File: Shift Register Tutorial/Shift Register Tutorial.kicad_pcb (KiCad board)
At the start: 2 copper layers, 134.6 x 162.6 mm, 58 parts, among them J101 USB_A, Q201 2N3904, Q301 2N3904, Q401 2N3904, SW201 SW_Push, SW301 SW_Push, SW401 SW_Push, U101 74164, U102 74164

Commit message: Some adjustments
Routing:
- net +5V: track 30.8 -> 0.00 mm, vias 8 -> 0
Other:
- outline, holes or cut-outs redrawn
- board text added: "Chained Shift Registers"

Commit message: Final tweaks
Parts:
- moved C201 6.35 mm to (-57.1, -52.1)
- moved D201 6.35 mm to (-47.0, -43.2)
- moved D401 6.35 mm to (-47.0, 33.0)
- moved Q201 6.35 mm to (-47.0, -34.3)
- moved R201 6.35 mm to (-57.1, -47.0)
- moved R202 6.35 mm to (-57.1, -36.8)
- moved R203 6.35 mm to (-52.1, -47.0)
- moved R301 6.35 mm to (-57.1, -11.4)
- moved R303 6.35 mm to (-52.1, -11.4)
- moved R401 6.35 mm to (-57.1, 19.1)
- moved R402 6.35 mm to (-57.1, 29.2)
- moved R403 6.35 mm to (-52.1, 19.1)
- moved SW201 6.35 mm to (-68.6, -45.7)
- moved SW301 6.35 mm to (-68.6, -10.2)
- moved SW401 6.35 mm to (-68.6, 30.5)
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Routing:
- net /Data/DATA: track 79.4 -> 72.7 mm
- net /Clock/CLOCK: track 219.3 -> 224.2 mm
- net /~RESET/~RESET: track 209.8 -> 209.1 mm
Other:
- board size 134.6 x 162.6 mm -> 133.3 x 156.2 mm
- board text added: "Debounce"
- board text added: "JLCJLCJLCJLC"
- board text added: "RGE2021"

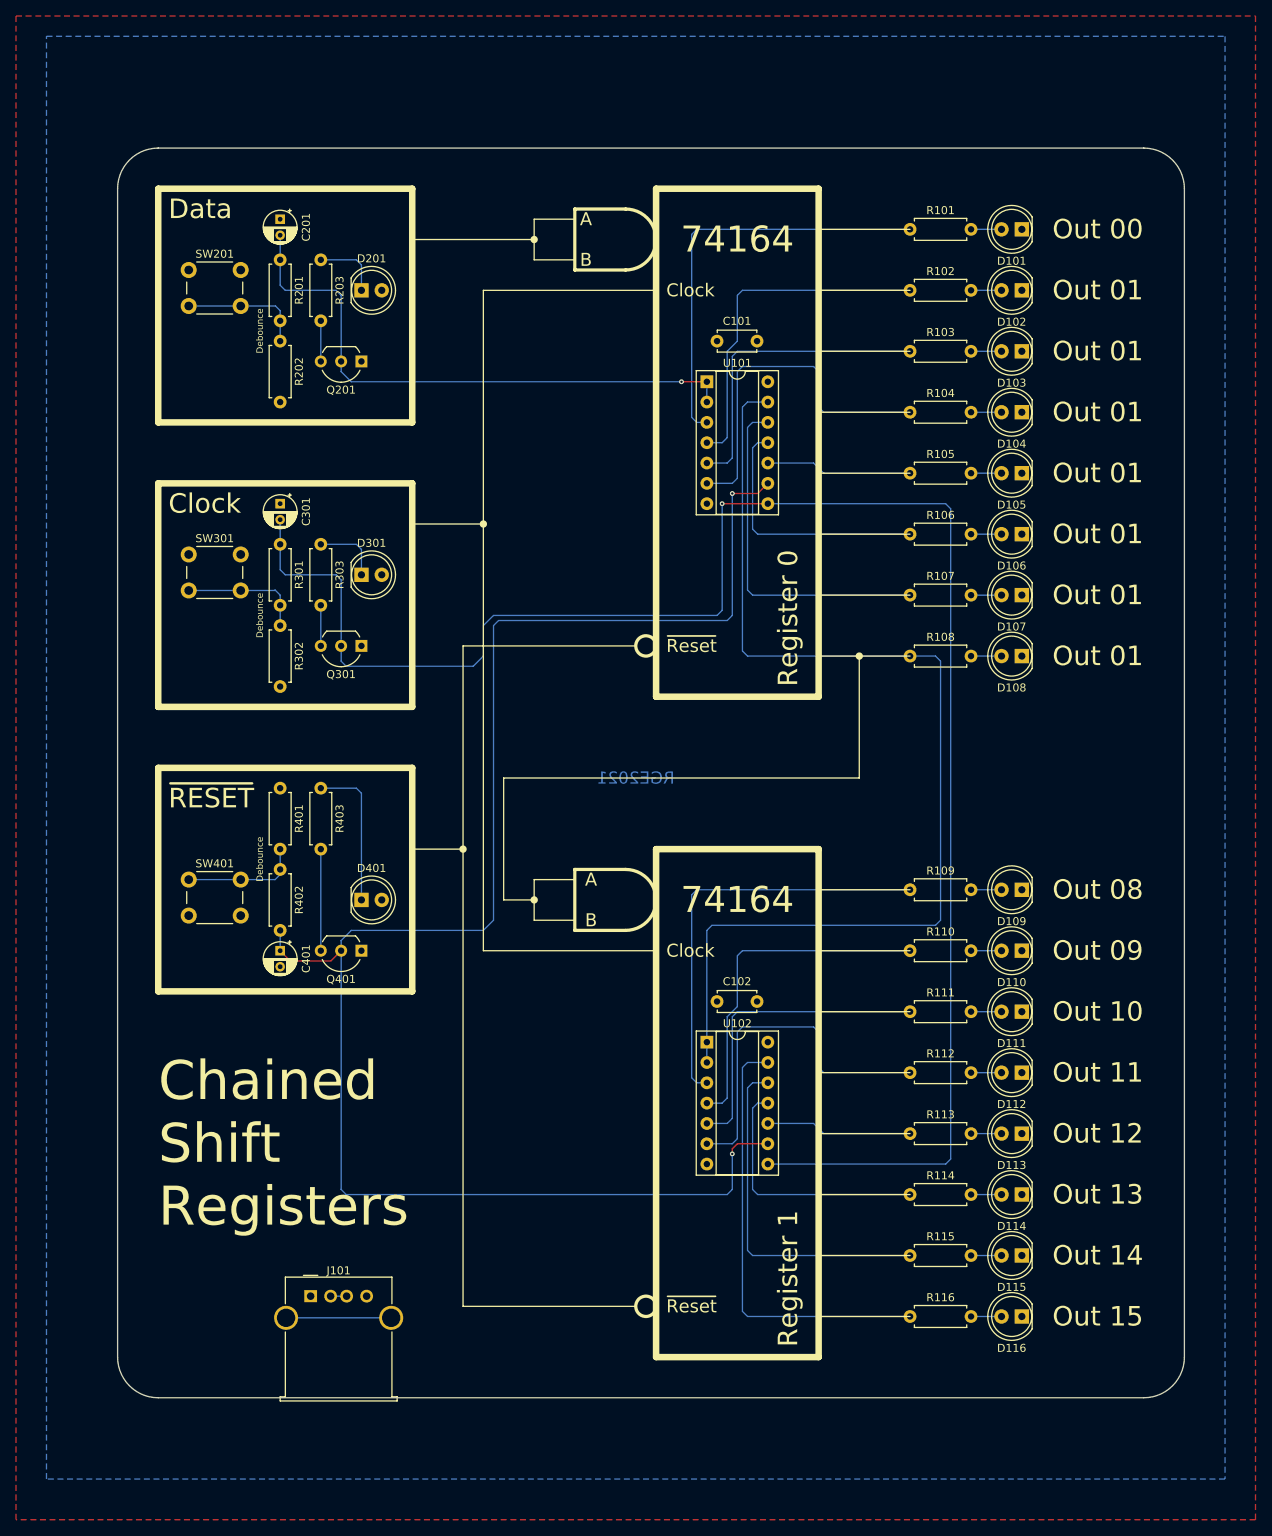
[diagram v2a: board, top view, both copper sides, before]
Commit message: Fix shift register tutorial (#11)
I had forgotten how NPN transistors worked, which resulted in the push buttons not affecting their target pins. Remove the transistors & indicator LEDs, and shrink the board.
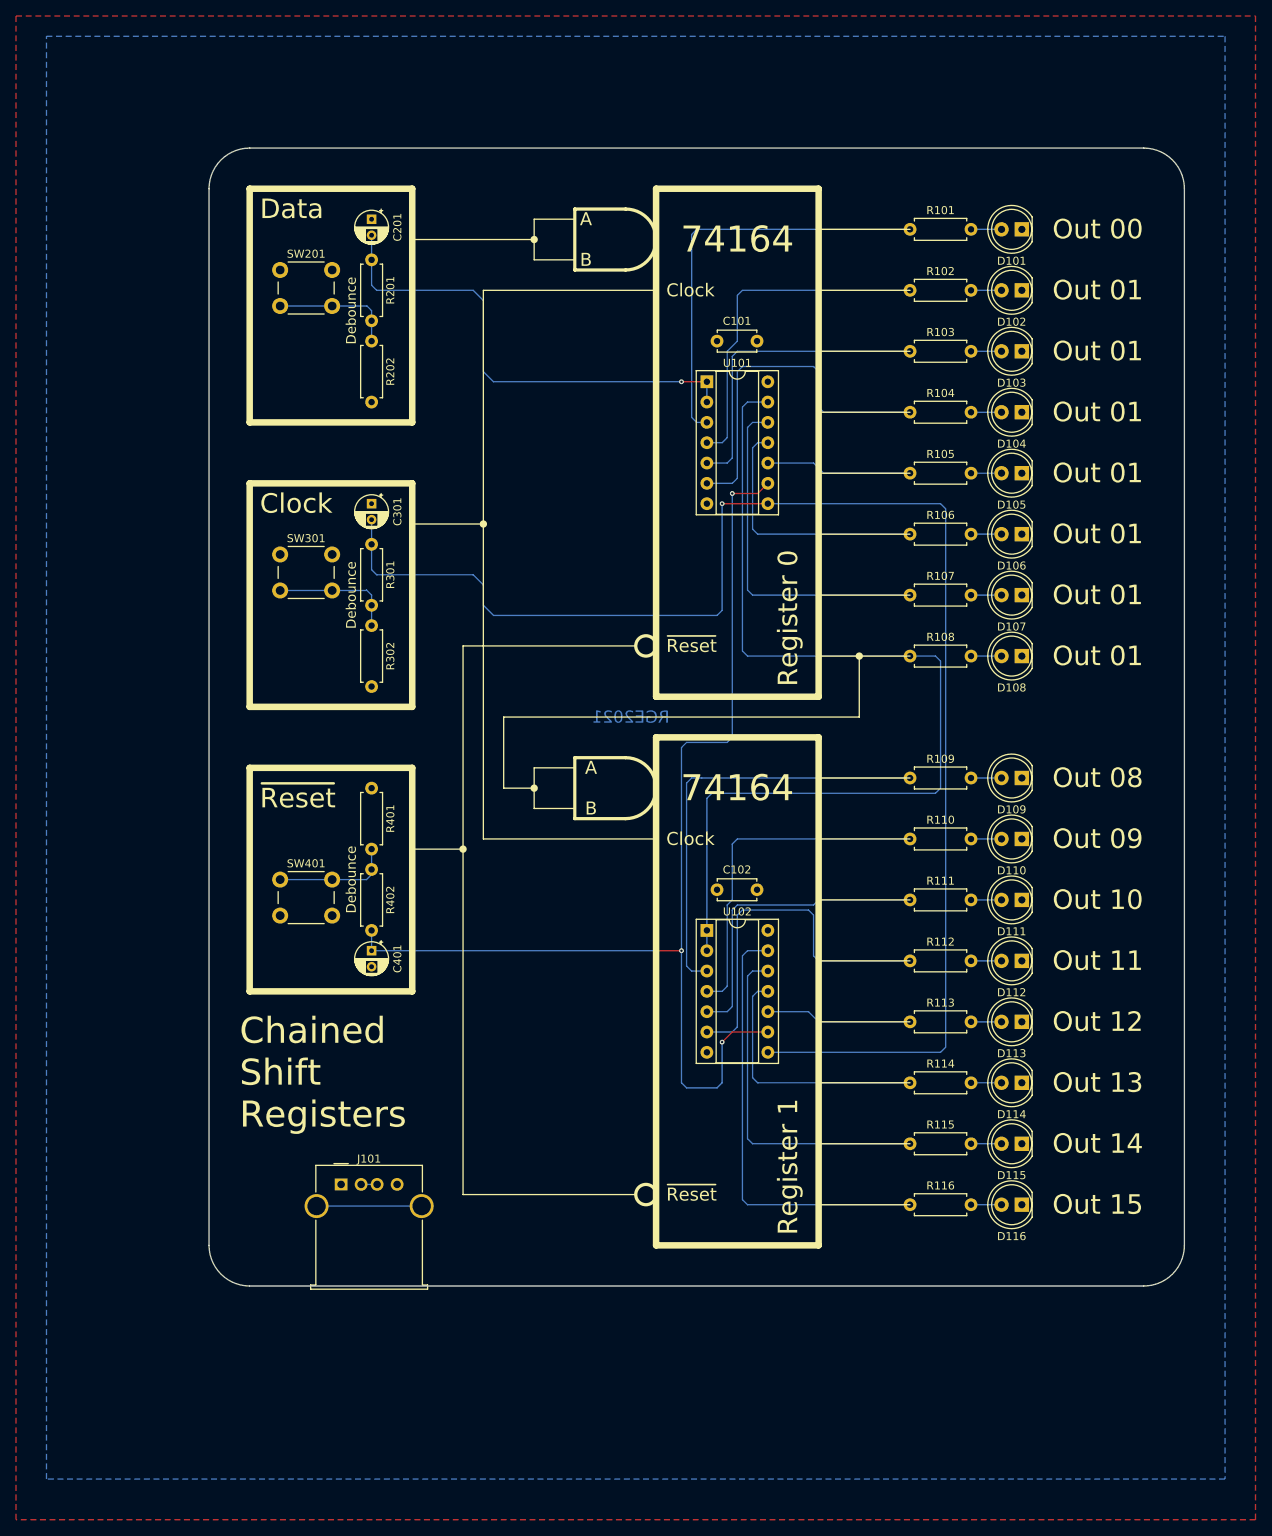
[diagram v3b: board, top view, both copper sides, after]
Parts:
- removed D201, D301, D401: LED, LED_THT:LED_D5.0mm
- removed Q201, Q301, Q401: 2N3904, Package_TO_SOT_THT:TO-92_Inline_Wide
- removed R203, R303, R403: 2k2, Resistor_THT:R_Axial_DIN0207_L6.3mm_D2.5mm_P7.62mm_Horizontal
- C201, C301, C401: value 1u -> 10u
- moved J101 14.5 mm to (-49.5, 68.6)
- moved C102 14.0 mm to (-2.54, 31.8)
- moved D109 14.0 mm to (35.6, 17.8)
- moved D110 14.0 mm to (35.6, 25.4)
- moved D111 14.0 mm to (35.6, 33.0)
- moved D112 14.0 mm to (35.6, 40.6)
- moved D113 14.0 mm to (35.6, 48.3)
- moved D115 14.0 mm to (35.6, 63.5)
- moved D116 14.0 mm to (35.6, 71.1)
- moved R109 14.0 mm to (21.6, 17.8)
- moved R110 14.0 mm to (21.6, 25.4)
- moved R111 14.0 mm to (21.6, 33.0)
- moved R112 14.0 mm to (21.6, 40.6)
- moved R113 14.0 mm to (21.6, 48.3)
- moved R115 14.0 mm to (21.6, 63.5)
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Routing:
- net /~RESET/~RESET: track 209.1 -> 142.4 mm, vias 2 -> 4
- net /Clock/CLOCK: track 224.2 -> 185.5 mm
- net Net-(D401-Pad1): track 18.7 -> 0.00 mm
- net Net-(R108-Pad1): track 137.8 -> 123.9 mm
- net Net-(Q401-Pad3): track 12.7 -> 0.00 mm
- net /Data/DATA: track 72.7 -> 60.9 mm
- net Net-(D301-Pad1): track 8.52 -> 0.00 mm
- net Net-(D201-Pad1): track 8.52 -> 0.00 mm
- net Net-(Q301-Pad3): track 5.08 -> 0.00 mm
- net Net-(Q201-Pad3): track 5.08 -> 0.00 mm
- net Net-(R112-Pad1): track 44.2 -> 45.5 mm
- net Net-(R109-Pad1): track 52.6 -> 53.9 mm
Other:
- board size 133.3 x 156.2 mm -> 121.9 x 142.2 mm
- board text removed: "~RESET"

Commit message: Removing old things
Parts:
- removed C201, C401: 10u, Capacitor_THT:CP_Radial_D4.0mm_P2.00mm
- removed R202: 10k, Resistor_THT:R_Axial_DIN0207_L6.3mm_D2.5mm_P7.62mm_Horizontal
- removed the R401 at (-45.7, 19.1)
- renumbered R402 to R401
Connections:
- R201 pad 2: Net-(R201-Pad2) -> GND
- R401 pad 1: Net-(R401-Pad2) -> +5V
- SW201 pad 1: +5V -> /Data/DATA
- SW201 pad 2: Net-(R201-Pad2) -> +5V
- SW401 pad 1: Net-(R401-Pad2) -> GND
- SW401 pad 2: GND -> /~RESET/~RESET
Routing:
- net /~RESET/~RESET: track 142.4 -> 104.3 mm
- net /Clock/CLOCK: track 185.5 -> 160.2 mm
- net /Data/DATA: track 60.9 -> 41.7 mm
- net Net-(R301-Pad2): track 15.5 -> 0.00 mm
- net Net-(R201-Pad2): track 15.5 -> 0.00 mm
- net Net-(R401-Pad2): track 14.9 -> 0.00 mm

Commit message: Working circuit together
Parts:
- added C302: 0.1u, Capacitor_THT:C_Disc_D4.7mm_W2.5mm_P5.00mm, F.Cu at (-44.5, -3.81)
- added U301: LM555xM, Package_DIP:DIP-8_W7.62mm_Socket, F.Cu at (-57.1, -3.81)
- C301: value 10u -> 10nF; footprint Capacitor_THT:CP_Radial_D4.0mm_P2.00mm -> Capacitor_THT:C_Disc_D3.0mm_W2.0mm_P2.50mm
- R302: value 10k -> 1M
- moved C301 20.4 mm to (-44.5, 3.81), turned to 90 degrees
- moved R302 13.7 mm to (-57.1, -8.89), turned to 0 degrees
- moved SW301 12.7 mm to (-57.1, -22.9)
- moved SW401 6.35 mm to (-57.1, 24.1)
- moved R301 5.08 mm to (-45.7, -16.5), turned to 90 degrees
- moved R201 2.54 mm to (-45.7, -49.5)
- moved SW201 2.54 mm to (-57.1, -48.3)
- moved R401 1.27 mm to (-45.7, 30.5), turned to 90 degrees
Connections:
- C301 pad 1: +5V -> Net-(C301-Pad1)
- C301 pad 2: /Clock/CLOCK -> GND
- R301 pad 1: /Clock/CLOCK -> +5V
- R302 pad 1: Net-(R301-Pad2) -> +5V
- R302 pad 2: GND -> Net-(C302-Pad2)
- R401 pad 1: +5V -> /~RESET/~RESET
- R401 pad 2: /~RESET/~RESET -> +5V
- SW301 pad 1: +5V -> Net-(R301-Pad2)
- SW301 pad 2: Net-(R301-Pad2) -> GND

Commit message: Ordered design
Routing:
- net /~RESET/~RESET: track 104.3 -> 160.2 mm
- net /Clock/CLOCK: track 160.2 -> 212.0 mm
- net Net-(R301-Pad2): track 0.00 -> 37.1 mm
- net /Data/DATA: track 41.7 -> 72.7 mm
- net Net-(C302-Pad2): track 0.00 -> 18.9 mm
- net Net-(C301-Pad1): track 0.00 -> 5.08 mm
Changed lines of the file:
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@@
     (thickness 1.6)
     (drawings 113)
-    (tracks 160)
+    (tracks 193)
     (zones 0)
     (modules 47)
@@
     (effects (font (size 1.2192 1.2192) (thickness 0.1524)))
   )
-  (gr_text RGE2021 (at -13.335 10.16) (layer B.Cu)
+  (gr_text RGE2021 (at -21.59 -3.81) (layer B.Cu)
     (effects (font (size 1.524 1.524) (thickness 0.3048)) (justify mirror))
   )
@@
   (segment (start -30.48 -31.75) (end -31.75 -33.02) (width 0.127) (layer B.Cu) (net 37))
   (segment (start -31.75 -33.02) (end -31.75 -41.91) (width 0.127) (layer B.Cu) (net 37))
-  (segment (start -31.75 -41.91) (end -33.02 -43.18) (width 0.127) (layer B.Cu) (net 37))
+  (segment (start -57.15 -48.26) (end -50.65 -48.26) (width 0.127) (layer B.Cu) (net 37))
+  (segment (start -50.65 -48.26) (end -49.53 -49.38) (width 0.127) (layer B.Cu) (net 37))
+  (segment (start -45.87 -49.38) (end -45.72 -49.53) (width 0.127) (layer B.Cu) (net 37))
+  (segment (start -49.53 -49.38) (end -45.87 -49.38) (width 0.127) (layer B.Cu) (net 37))
+  (segment (start -45.72 -49.53) (end -33.02 -49.53) (width 0.127) (layer B.Cu) (net 37))
+  (segment (start -33.02 -49.53) (end -31.75 -48.26) (width 0.127) (layer B.Cu) (net 37))
+  (segment (start -31.75 -48.26) (end -31.75 -41.91) (width 0.127) (layer B.Cu) (net 37))
   (segment (start 3.81 -16.51) (end 0 -16.51) (width 0.127) (layer F.Cu) (net 38))
   (segment (start 0 -16.51) (end -1.905 -16.51) (width 0.127) (layer F.Cu) (net 38))
   (segment (start -1.905 -16.51) (end -1.905 -16.51) (width 0.127) (layer F.Cu) (net 38))
   (via (at -1.905 -16.51) (size 0.6) (drill 0.3) (layers F.Cu B.Cu) (net 38))
-  (segment (start -2.54 -2.54) (end -1.905 -3.175) (width 0.127) (layer B.Cu) (net 38))
-  (segment (start -1.905 -3.175) (end -1.905 -16.51) (width 0.127) (layer B.Cu) (net 38))
-  (segment (start -2.54 -2.54) (end -30.48 -2.54) (width 0.127) (layer B.Cu) (net 38))
   (segment (start 25.4 -16.51) (end 3.81 -16.51) (width 0.127) (layer B.Cu) (net 38))
   (segment (start 26.035 -15.875) (end 25.4 -16.51) (width 0.127) (layer B.Cu) (net 38))
@@
   (segment (start 25.4 52.07) (end 26.035 51.435) (width 0.127) (layer B.Cu) (net 38))
   (segment (start 3.81 52.07) (end 25.4 52.07) (width 0.127) (layer B.Cu) (net 38))
+  (segment (start -58.42 1.27) (end -57.15 1.27) (width 0.127) (layer B.Cu) (net 38))
+  (segment (start -59.69 2.54) (end -58.42 1.27) (width 0.127) (layer B.Cu) (net 38))
+  (segment (start -59.69 8.89) (end -59.69 2.54) (width 0.127) (layer B.Cu) (net 38))
+  (segment (start -58.42 10.16) (end -59.69 8.89) (width 0.127) (layer B.Cu) (net 38))
+  (segment (start -2.54 10.16) (end -58.42 10.16) (width 0.127) (layer B.Cu) (net 38))
+  (segment (start -1.905 9.525) (end -2.54 10.16) (width 0.127) (layer B.Cu) (net 38))
+  (segment (start -1.905 -16.51) (end -1.905 9.525) (width 0.127) (layer B.Cu) (net 38))
+  (segment (start -49.38 -24.13) (end -50.65 -22.86) (width 0.127) (layer B.Cu) (net 39))
+  (segment (start -45.72 -24.13) (end -49.38 -24.13) (width 0.127) (layer B.Cu) (net 39))
+  (segment (start -50.65 -22.86) (end -57.15 -22.86) (width 0.127) (layer B.Cu) (net 39))
+  (segment (start -57.15 -1.27) (end -58.42 -1.27) (width 0.127) (layer B.Cu) (net 39))
+  (segment (start -58.42 -1.27) (end -59.69 -2.54) (width 0.127) (layer B.Cu) (net 39))
+  (segment (start -59.69 -2.54) (end -59.69 -21.59) (width 0.127) (layer B.Cu) (net 39))
+  (segment (start -59.69 -21.59) (end -58.42 -22.86) (width 0.127) (layer B.Cu) (net 39))
+  (segment (start -58.42 -22.86) (end -57.15 -22.86) (width 0.127) (layer B.Cu) (net 39))
   (segment (start 3.81 -19.05) (end 2.54 -17.78) (width 0.127) (layer F.Cu) (net 40))
   (segment (start 2.54 -17.78) (end -0.635 -17.78) (width 0.127) (layer F.Cu) (net 40))
@@
   (via (at -6.985 39.37) (size 0.6) (drill 0.3) (layers F.Cu B.Cu) (net 40))
   (segment (start -10.16 39.37) (end -6.985 39.37) (width 0.127) (layer F.Cu) (net 40))
+  (segment (start -57.15 28.63) (end -50.65 28.63) (width 0.127) (layer B.Cu) (net 40))
+  (segment (start -47.57 28.63) (end -45.72 30.48) (width 0.127) (layer B.Cu) (net 40))
+  (segment (start -50.65 28.63) (end -47.57 28.63) (width 0.127) (layer B.Cu) (net 40))
+  (segment (start -10.16 39.37) (end -44.45 39.37) (width 0.127) (layer B.Cu) (net 40))
+  (segment (start -44.45 39.37) (end -45.72 38.1) (width 0.127) (layer B.Cu) (net 40))
+  (segment (start -45.72 38.1) (end -45.72 30.48) (width 0.127) (layer B.Cu) (net 40))
+  (segment (start -49.53 1.27) (end -49.53 -1.27) (width 0.127) (layer B.Cu) (net 41))
+  (segment (start -49.53 -1.27) (end -50.8 -1.27) (width 0.127) (layer B.Cu) (net 41))
+  (segment (start -50.8 -1.27) (end -52.07 -2.54) (width 0.127) (layer B.Cu) (net 41))
+  (segment (start -52.07 -2.54) (end -52.07 -7.62) (width 0.127) (layer B.Cu) (net 41))
+  (segment (start -52.07 -7.62) (end -50.8 -8.89) (width 0.127) (layer B.Cu) (net 41))
+  (segment (start -50.8 -8.89) (end -49.53 -8.89) (width 0.127) (layer B.Cu) (net 41))
+  (segment (start -44.53 -8.89) (end -44.45 -8.81) (width 0.127) (layer B.Cu) (net 41))
+  (segment (start -49.53 -8.89) (end -44.53 -8.89) (width 0.127) (layer B.Cu) (net 41))
+  (segment (start -49.53 3.81) (end -44.45 3.81) (width 0.127) (layer B.Cu) (net 42))
   (zone (net 20) (net_name +5V) (layer B.Cu) (hatch edge 0.508)
     (connect_pads (clearance 0.254))
     (min_thickness 0.127)
-    (fill (arc_segments 32) (thermal_gap 0.508) (thermal_bridge_width 0.508))
+    (fill yes (arc_segments 32) (thermal_gap 0.508) (thermal_bridge_width 0.508))
     (polygon
       (pts
@@
     (connect_pads (clearance 0.254))
     (min_thickness 0.127)
-    (fill (arc_segments 32) (thermal_gap 0.508) (thermal_bridge_width 0.508))
+    (fill yes (arc_segments 32) (thermal_gap 0.508) (thermal_bridge_width 0.508))
     (polygon
       (pts
